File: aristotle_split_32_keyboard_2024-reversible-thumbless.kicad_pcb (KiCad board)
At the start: 2 copper layers, 100 x 87.7 mm, 43 parts, among them J1 8P8C, J2 Screw_Terminal_01x04, J3 Screw_Terminal_01x04, K13 SW_SPDT, K14 SW_SPDT, K15 SW_SPDT, K16 SW_SPDT, K17 SW_SPDT, K23 SW_SPDT, K24 SW_SPDT, K25 SW_SPDT, K26 SW_SPDT, K27 SW_SPDT, K4 SW_SPDT, K5 SW_SPDT, K6 SW_SPDT, K7 SW_SPDT, SW1 SW_SPDT, U1 ProMicro_r

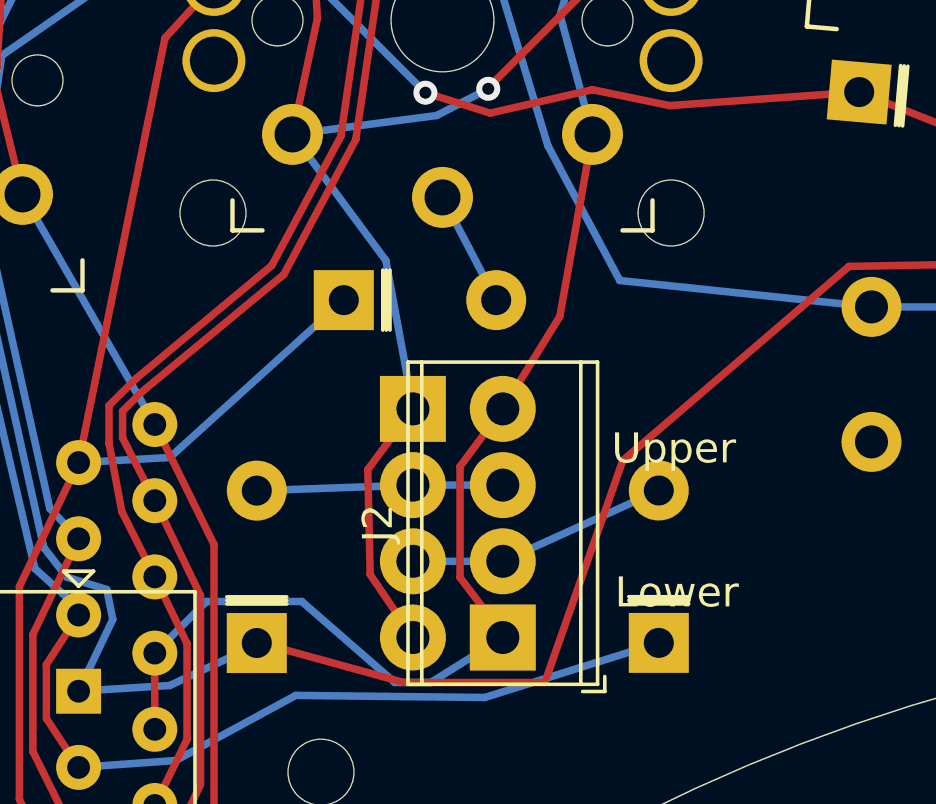
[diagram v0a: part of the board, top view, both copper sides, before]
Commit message: Fix mounting holes
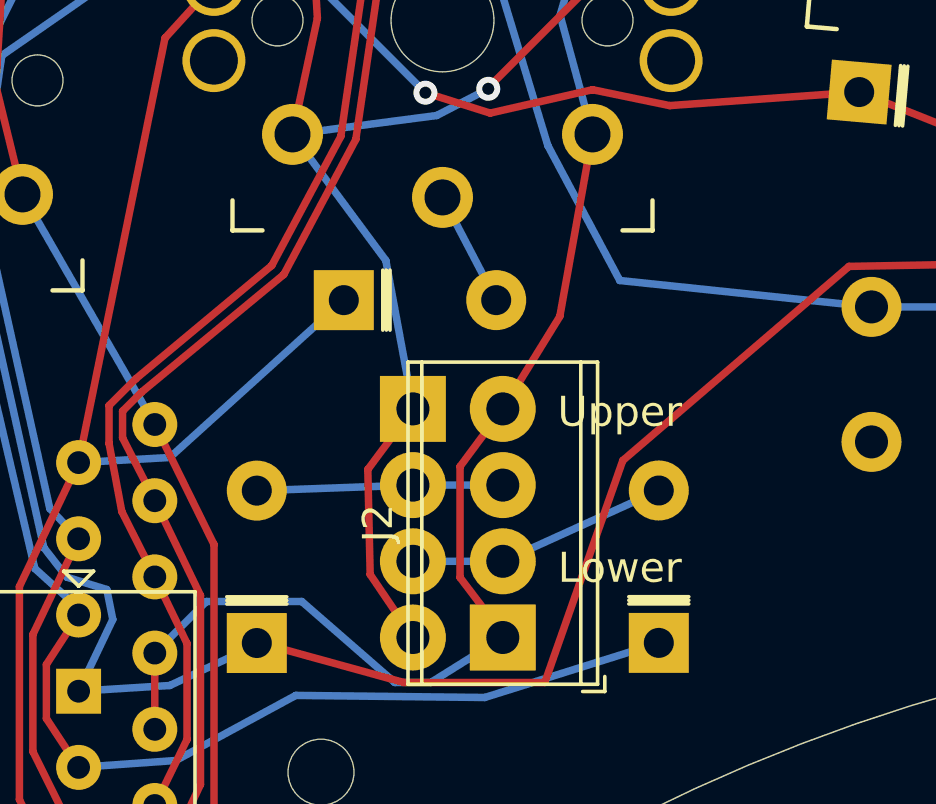
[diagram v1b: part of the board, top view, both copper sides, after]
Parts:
- removed the H3 at (115.3, 130.4)
- removed the H4 at (100.0, 130.4)
- U1: value ProMicro_r -> Nice Nano
- renumbered H4 to H1, H4 to H2, H4 to H3
